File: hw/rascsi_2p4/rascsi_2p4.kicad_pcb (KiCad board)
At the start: 2 copper layers, 65 x 56 mm, 95 parts, among them IC1 SN74LS641-1DW, IC2 SN74LS641-1DW, IC3 SN74LS641-1DW, IC4 SN74LS641-1DW, J1 Raspberry_Pi_2_3, J2 DNP, J3 Conn_02x25_Odd_Even, J4 I2C Pinout, J5 DNP, J6 CONNFLY DB-25, J7 DNP, J8 USB_B_Micro, J9 Conn_02x25_Odd_Even, X1 Mac, X2 Dogcow, X3 Mac, X4 Dogcow, X5 Dogcow, X6 Dogcow, X7 Pi, X8 Pi

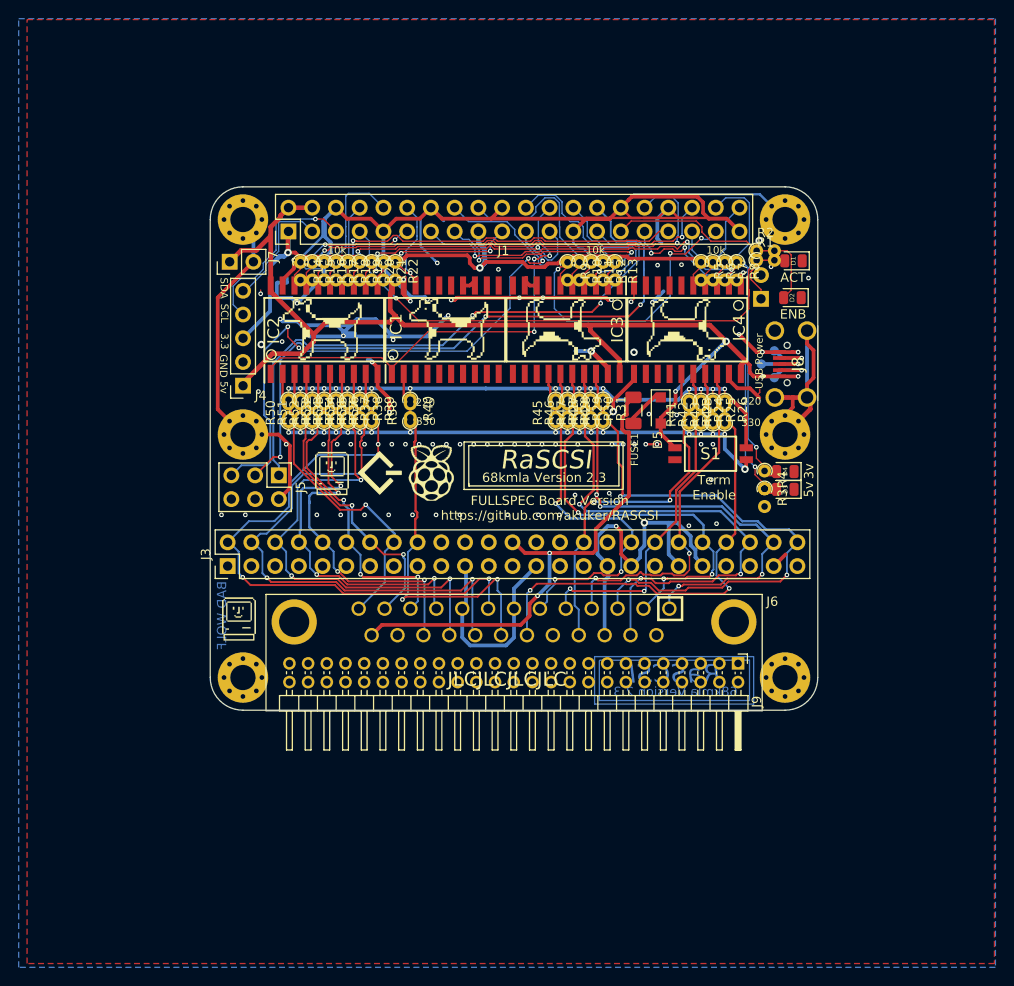
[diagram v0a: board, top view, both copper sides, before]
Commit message: Clean up silkscreen and fix DRC issues
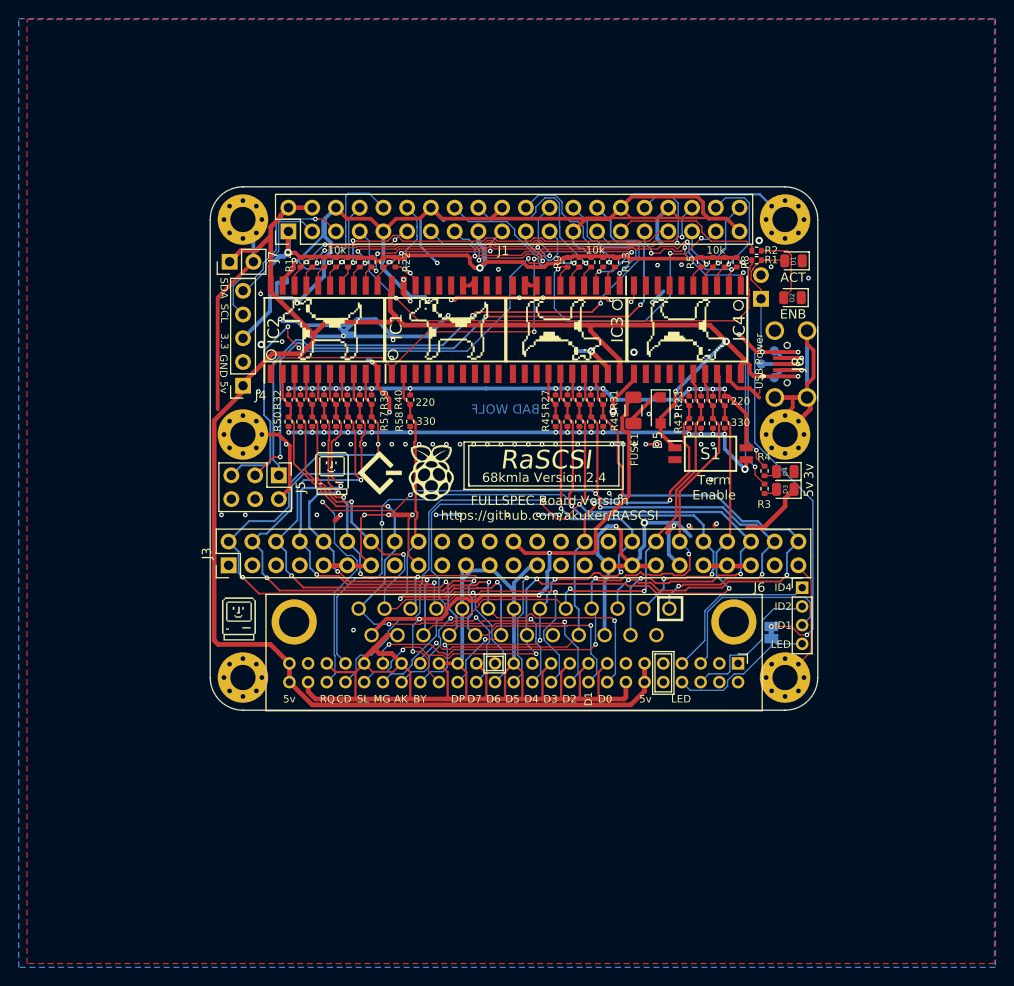
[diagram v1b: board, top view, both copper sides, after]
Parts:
- added J10: Conn_01x04_Male, Connector_PinHeader_2.00mm:PinHeader_1x04_P2.00mm_Vertical, F.Cu at (237.8, 85.4)
- added JP1: SolderJumper_2_Bridged, Jumper:SolderJumper-2_P1.3mm_Bridged_Pad1.0x1.5mm, B.Cu at (234.5, 90.2)
- R1, R10, R11, R12, R13, R14, R15, R16, R17, R18, R19, R2, R20, R21, R22, R23, R24, R25, R26, R27, R28, R29, R3, R30, R31, R32, R33, R34, R35, R36, R37, R38, R39, R4, R40, R41, R42, R43, R44, R45, R46, R47, R48, R49, R5, R50, R51, R52, R53, R54, R55, R56, R57, R58, R6, R7, R8, R9: footprint Resistor_THT:R_Axial_DIN0204_L3.6mm_D1.6mm_P1.90mm_Vertical -> Resistor_SMD:R_0402_1005Metric
- moved J3 0.13 mm to (176.5, 83.0)
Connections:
- J9 pad 5: (no net) -> PB_SCSIID_1
- J9 pad 6: (no net) -> PB_SCSIID_2
- J9 pad 7: (no net) -> PB_SCSIID_4
- J9 pad 8: (no net) -> PB_LED_Pin
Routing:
- net GND: track 390.5 -> 556.8 mm, vias 82 -> 81
- net +5V: track 134.8 -> 216.9 mm
- net C-REQ: track 51.7 -> 104.8 mm, vias 4 -> 6
- net C-I_O: track 61.6 -> 108.8 mm, vias 3 -> 4
- net EXT-ACT-LED: track 7.56 -> 50.8 mm, vias 0 -> 2
- net C-C_D: track 57.4 -> 98.8 mm, vias 3 -> 4
- net C-MSG: track 45.5 -> 83.1 mm
- net C-RST: track 38.4 -> 67.8 mm, vias 2 -> 4
- net C-D3: track 44.3 -> 68.8 mm, vias 3 -> 4
- net C-SEL: track 52.4 -> 76.2 mm, vias 2 -> 4
- net C-ACK: track 36.5 -> 60.0 mm, vias 2 -> 3
- net C-D5: track 35.9 -> 58.7 mm, vias 3 -> 4
- net C-D7: track 34.3 -> 56.7 mm, vias 1 -> 3
- net C-D6: track 33.1 -> 54.7 mm, vias 2 -> 3
- net C-D0: track 66.8 -> 87.7 mm, vias 4 -> 5
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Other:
- board text added: "68kmla Version 2.4"
- board text added: "AK"
- board text added: "BY"
- board text added: "CD"
- board text added: "ID1"
- board text added: "ID2"
- board text added: "ID4"
- board text added: "IO"
- board text added: "LED"
- board text added: "MG"
- board text added: "RQ"
- board text added: "SL"
- board text removed: "68kmla Version 2.3"
- board text removed: "Only use the DB-25 OR 50-pin ribbon connector. DO NOT USE BOTH (Unless you REALLY know what you're doing)"

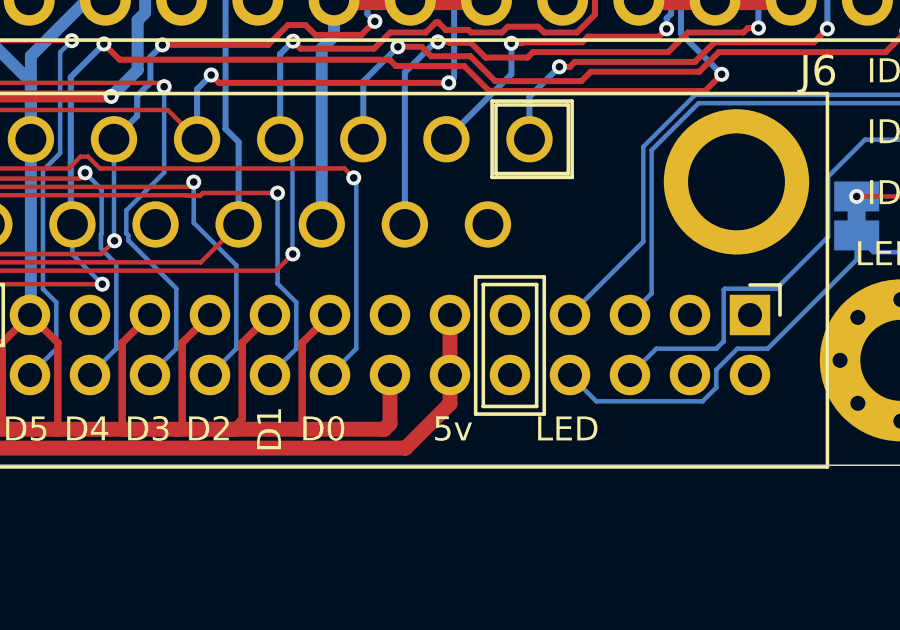
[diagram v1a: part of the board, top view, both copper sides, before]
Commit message: additional cleanup. Made Pin 1 of the PB connector square
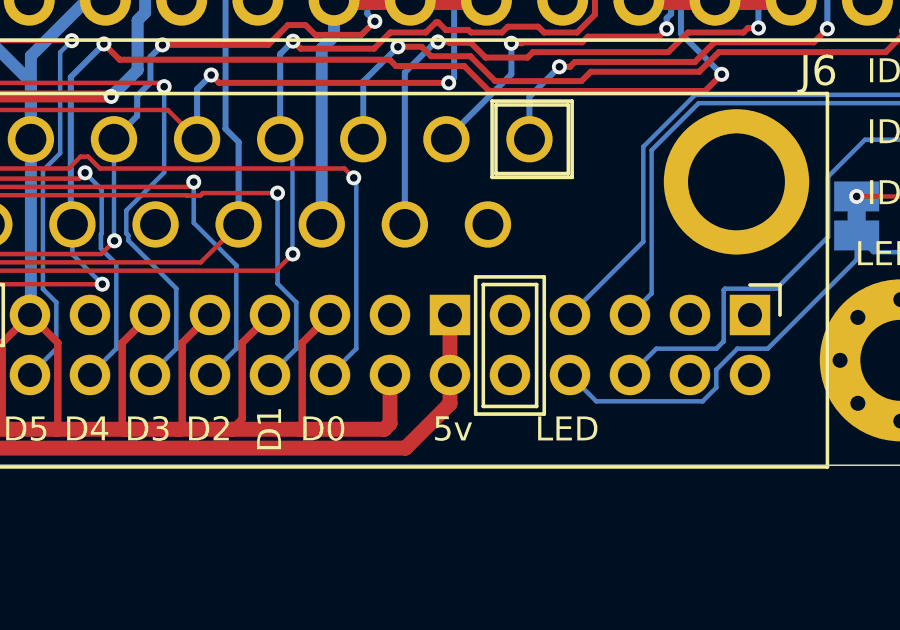
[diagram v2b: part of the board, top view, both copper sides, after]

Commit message: minor tweaks
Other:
- board text added: "J10"
- board text added: "J9"
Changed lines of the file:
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@@
   (general
     (thickness 1.6)
-    (drawings 289)
+    (drawings 293)
     (tracks 2096)
     (zones 0)
@@
     (descr "Through hole straight pin header, 2x25, 2.54mm pitch, double rows")
     (tags "Through hole pin header THT 2x25 2.54mm double row")
-    (fp_text reference J3 (at 1.27 -2.33 90) (layer F.SilkS)
+    (fp_text reference J3 (at 4.4925 0.1495 180) (layer F.SilkS)
       (effects (font (size 1 1) (thickness 0.15)))
     )
@@
     (descr U254-051N-4BH806-2)
     (tags Connector)
-    (fp_text reference J8 (at 0 0 90) (layer F.SilkS)
+    (fp_text reference J8 (at 0.738 1.202 90) (layer F.SilkS)
       (effects (font (size 1.27 1.27) (thickness 0.254)))
     )
@@
     )
   )
+  (gr_text J10 (at 236.306 86.122 90) (layer B.SilkS)
+    (effects (font (size 1 1) (thickness 0.15)) (justify mirror))
+  )
+  (gr_text J9 (at 226.4 91.71) (layer B.SilkS)
+    (effects (font (size 1 1) (thickness 0.15)) (justify mirror))
+  )
+  (gr_text J10 (at 234.274 87.9 90) (layer F.SilkS)
+    (effects (font (size 1 1) (thickness 0.15)))
+  )
+  (gr_text J10 (at 187.538 87.392) (layer F.SilkS)
+    (effects (font (size 1 1) (thickness 0.15)))
+  )
+  (gr_text J9 (at 181.188 92.726) (layer F.SilkS)
+    (effects (font (size 1 1) (thickness 0.15)))
+  )
   (gr_line (start 203.794 94.504) (end 203.794 92.472) (layer B.SilkS) (width 0.12))
   (gr_line (start 206.08 94.504) (end 203.794 94.504) (layer B.SilkS) (width 0.12))
@@
     (effects (font (size 1 1) (thickness 0.15)) (justify mirror))
   )
-  (gr_text J8 (at 237.363 61.4045 90) (layer B.SilkS)
+  (gr_text J8 (at 236.306 61.23 90) (layer B.SilkS)
     (effects (font (size 1.27 1.27) (thickness 0.23)) (justify mirror))
   )
@@
     (effects (font (size 0.8 0.8) (thickness 0.15)) (justify mirror))
   )
-  (gr_text J6 (at 235.798 85.614 270) (layer B.SilkS)
+  (gr_text J6 (at 225.892 86.376) (layer B.SilkS)
     (effects (font (size 1 1) (thickness 0.15)) (justify mirror))
   )
-  (gr_text J6 (at 233.258 85.36) (layer F.SilkS)
-    (effects (font (size 1 1) (thickness 0.15)))
-  )
   (gr_text RaSCSI (at 205.4375 56.862) (layer B.SilkS)

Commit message: Updates for ordered version
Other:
- rule pad_to_mask_clearance: 0.05 -> 0

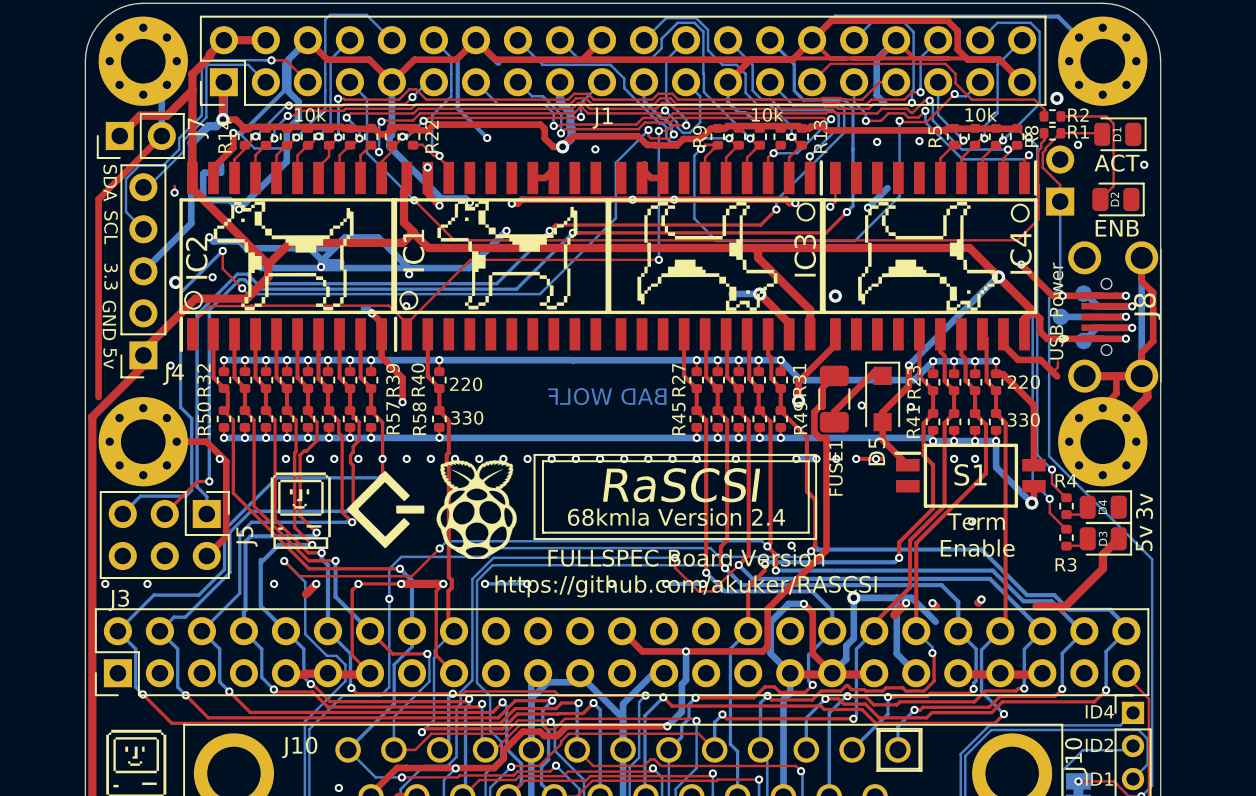
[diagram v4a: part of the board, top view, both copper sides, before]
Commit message: Added optional floppy power connector. As-ordered version 2.4a
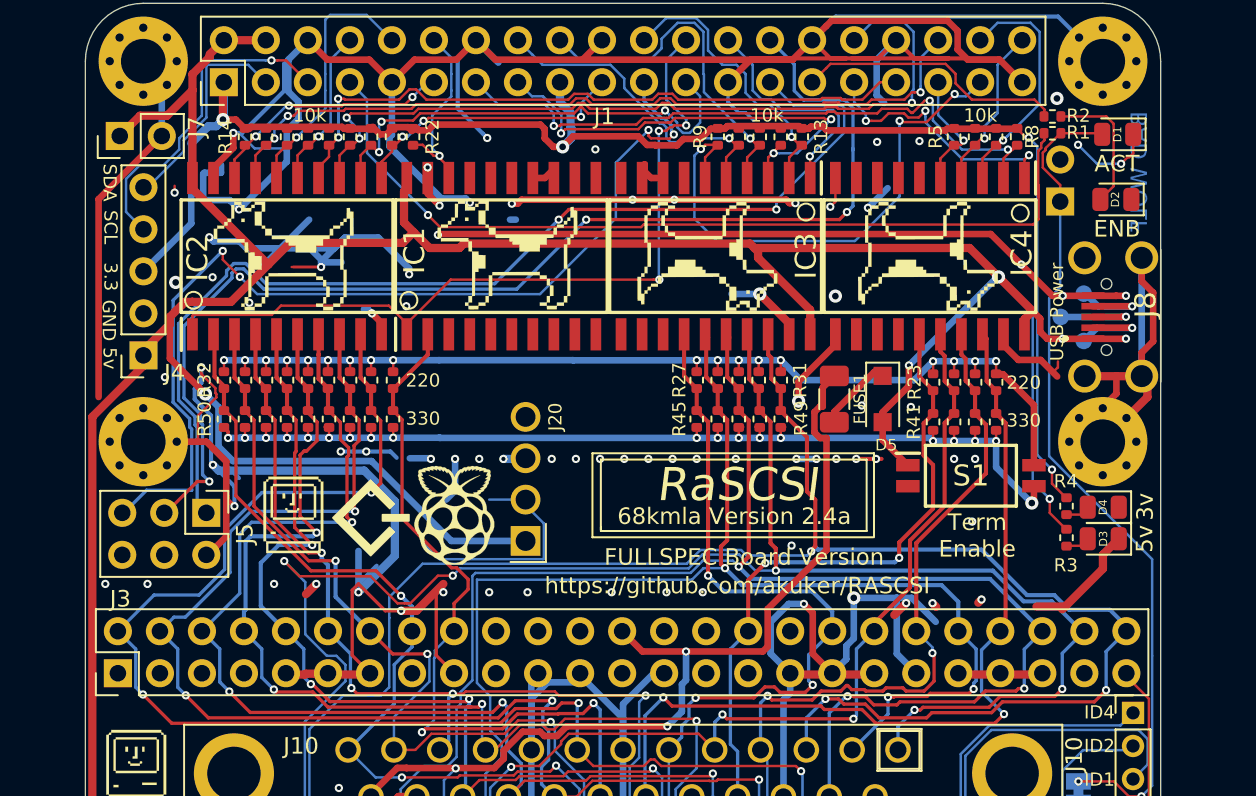
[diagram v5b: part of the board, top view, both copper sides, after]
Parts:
- added J20: 171826-4, SamacSys_Parts:SHDRRA4W69P0X250_1X4_1000X1350X670P, F.Cu at (201.1, 75.0)
- moved R40 2.80 mm to (193.1, 65.3)
- moved R58 2.80 mm to (193.1, 67.6)
- moved X7 1.39 mm to (196.8, 73.5)
- moved X8 1.01 mm to (191.6, 73.6)
- moved X3 0.51 mm to (187.1, 73.4)
- moved J5 0.08 mm to (181.8, 73.3)
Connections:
- J3 pad 25: (no net) -> Net-(J3-Pad25)
- J3 pad 34: (no net) -> Net-(J3-Pad34)
- J9 pad 1: (no net) -> Net-(J9-Pad1)
- J9 pad 10: (no net) -> Net-(J9-Pad10)
- J9 pad 2: (no net) -> Net-(J9-Pad2)
- J9 pad 27: (no net) -> Net-(J9-Pad27)
- J9 pad 3: (no net) -> Net-(J9-Pad3)
- J9 pad 4: (no net) -> Net-(J9-Pad4)
- J9 pad 9: (no net) -> Net-(J9-Pad9)
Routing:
- net GND: track 556.8 -> 643.5 mm, vias 81 -> 80
- net +5V: track 216.9 -> 247.2 mm, vias 5 -> 6
- net C-DP: track 51.0 -> 53.4 mm
- net PI_GPIO1: track 69.5 -> 71.8 mm
- net PI_GPIO0: track 63.4 -> 65.4 mm
- net C-REQ: track 104.8 -> 106.4 mm, vias 6 -> 5
- net C-C_D: track 98.8 -> 97.2 mm, vias 4 -> 3
- net C-I_O: track 108.8 -> 107.6 mm, vias 4 -> 3
- net C-D7: track 56.7 -> 55.7 mm
- net PI-DTD: track 48.0 -> 49.0 mm
- net C-D0: track 87.7 -> 86.8 mm, vias 5 -> 4
- net PI-ACT: track 54.2 -> 53.5 mm
- net (no net): vias 2 -> 1
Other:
- board text added: "68kmla Version 2.4a"
- board text removed: "68kmla Version 2.4"
